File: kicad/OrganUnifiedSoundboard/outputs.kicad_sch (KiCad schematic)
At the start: 9 parts, among them J10 Outputs 53-78, J12 Outputs 79-80, J8 Outputs 1-26, J9 Outputs 27-52

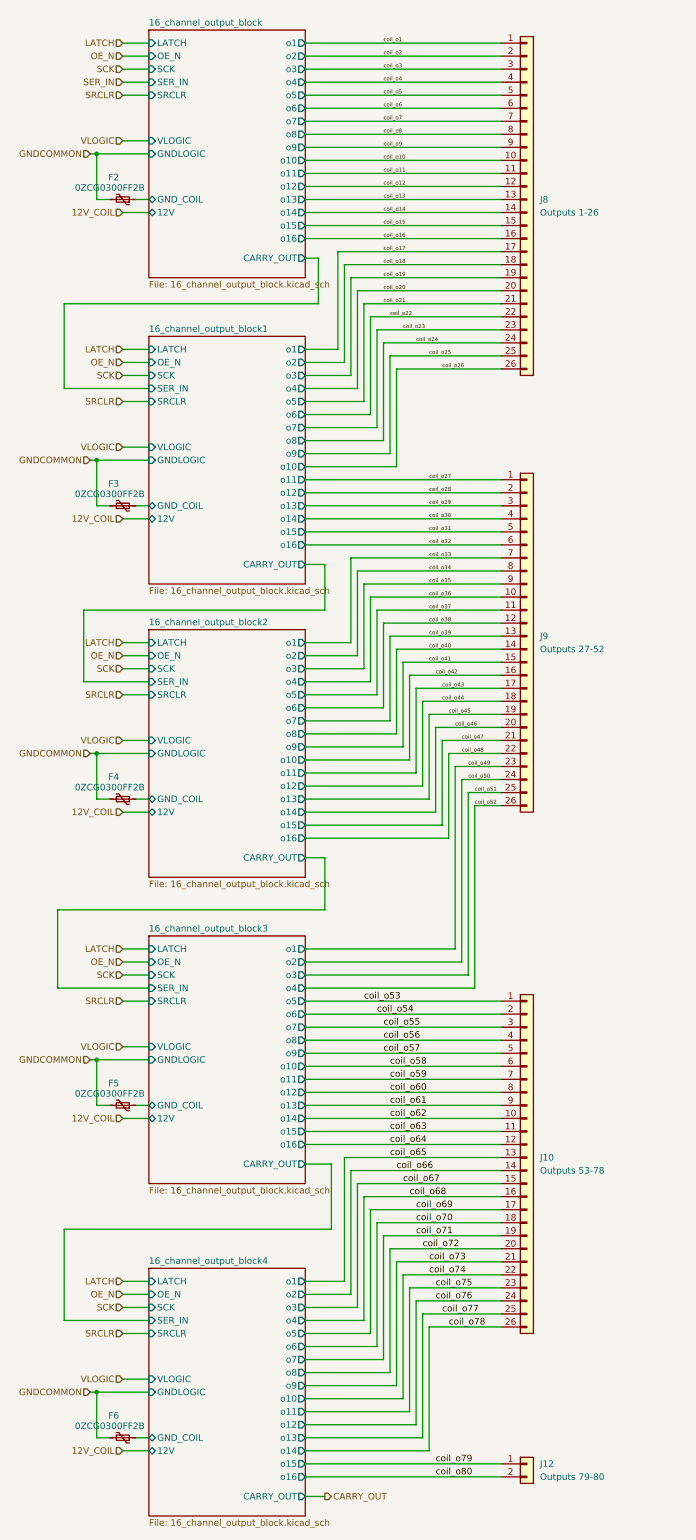
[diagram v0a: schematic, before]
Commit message: Finalized unified soundboard driver for production, adding some models
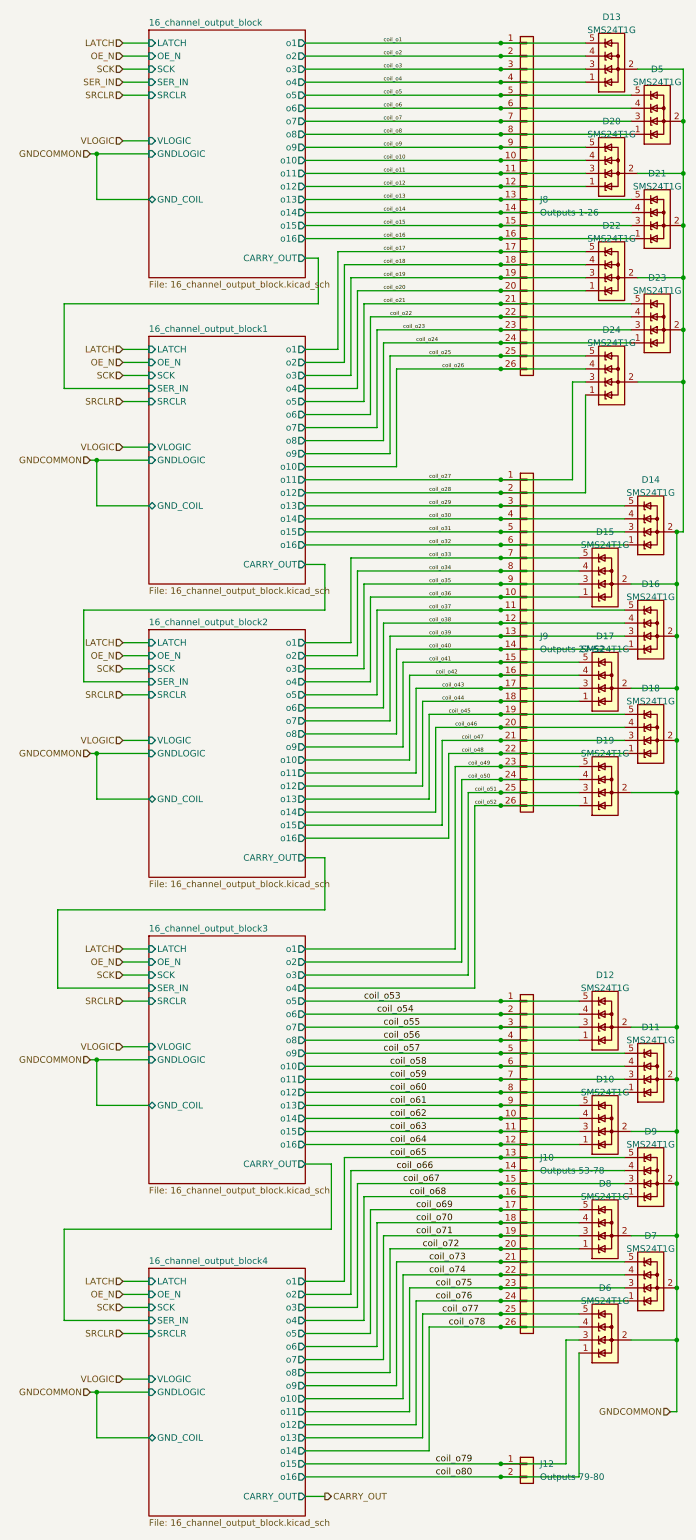
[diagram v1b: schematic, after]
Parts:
- removed F2, F3, F4, F5, F6: 0ZCG0300FF2B, Fuse:Fuse_1812_4532Metric, symbol Device:Polyfuse_Small
- added D10, D11, D12, D13, D14, D15, D16, D17, D18, D19, D20, D21, D22, D23, D24, D5, D6, D7, D8, D9: SMS24T1G, Package_TO_SOT_SMD:SOT-23-5, symbol Power_Protection:SP0504BAHT
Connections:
- net GNDCOMMON: now also D10.2 (A), D11.2 (A), D12.2 (A), D13.2 (A), D14.2 (A), D15.2 (A), D16.2 (A), D17.2 (A), D18.2 (A), D19.2 (A), D20.2 (A), D21.2 (A), D22.2 (A), D23.2 (A), D24.2 (A), D5.2 (A), D6.2 (A), D7.2 (A), D8.2 (A), D9.2 (A)
- net coil_o1: now also D13.5 (K)
- net coil_o10: now also D20.4 (K)
- net coil_o11: now also D20.3 (K)
- net coil_o12: now also D20.1 (K)
- net coil_o13: now also D21.5 (K)
- net coil_o14: now also D21.4 (K)
- net coil_o15: now also D21.3 (K)
- net coil_o16: now also D21.1 (K)
- net coil_o17: now also D22.5 (K)
- net coil_o18: now also D22.4 (K)
- net coil_o19: now also D22.3 (K)
- net coil_o2: now also D13.4 (K)
- net coil_o20: now also D22.1 (K)
- net coil_o21: now also D23.5 (K)
- net coil_o22: now also D23.4 (K)
- net coil_o23: now also D23.3 (K)
- net coil_o24: now also D23.1 (K)
- net coil_o25: now also D24.5 (K)
- net coil_o26: now also D24.4 (K)
- net coil_o27: now also D24.3 (K)
- net coil_o28: now also D24.1 (K)
- net coil_o29: now also D14.5 (K)
- net coil_o3: now also D13.3 (K)
- net coil_o30: now also D14.4 (K)
- net coil_o31: now also D14.3 (K)
- net coil_o32: now also D14.1 (K)
- net coil_o33: now also D15.5 (K)
- net coil_o34: now also D15.4 (K)
- net coil_o35: now also D15.3 (K)
- net coil_o36: now also D15.1 (K)
- net coil_o37: now also D16.5 (K)
- net coil_o38: now also D16.4 (K)
- net coil_o39: now also D16.3 (K)
- net coil_o4: now also D13.1 (K)
- net coil_o40: now also D16.1 (K)
- net coil_o41: now also D17.5 (K)
- net coil_o42: now also D17.4 (K)
- net coil_o43: now also D17.3 (K)
- net coil_o44: now also D17.1 (K)
- net coil_o45: now also D18.5 (K)
- net coil_o46: now also D18.4 (K)
- net coil_o47: now also D18.3 (K)
- net coil_o48: now also D18.1 (K)
- net coil_o49: now also D19.5 (K)
- net coil_o5: now also D5.5 (K)
- net coil_o50: now also D19.4 (K)
- net coil_o51: now also D19.3 (K)
- net coil_o52: now also D19.1 (K)
- net coil_o53: now also D12.5 (K)
- net coil_o54: now also D12.4 (K)
- net coil_o55: now also D12.3 (K)
- net coil_o56: now also D12.1 (K)
- net coil_o57: now also D11.5 (K)
- net coil_o58: now also D11.4 (K)
- net coil_o59: now also D11.3 (K)
- net coil_o6: now also D5.4 (K)
- net coil_o60: now also D11.1 (K)
- net coil_o61: now also D10.5 (K)
- net coil_o62: now also D10.4 (K)
- net coil_o63: now also D10.3 (K)
- net coil_o64: now also D10.1 (K)
- net coil_o65: now also D9.5 (K)
- net coil_o66: now also D9.4 (K)
- net coil_o67: now also D9.3 (K)
- net coil_o68: now also D9.1 (K)
- net coil_o69: now also D8.5 (K)
- net coil_o7: now also D5.3 (K)
- net coil_o70: now also D8.4 (K)
- net coil_o71: now also D8.3 (K)
- net coil_o72: now also D8.1 (K)
- net coil_o73: now also D7.5 (K)
- net coil_o74: now also D7.4 (K)
- net coil_o75: now also D7.3 (K)
- net coil_o76: now also D7.1 (K)
- net coil_o77: now also D6.5 (K)
- net coil_o78: now also D6.4 (K)
- net coil_o79: now also D6.3 (K)
- net coil_o8: now also D5.1 (K)
- net coil_o80: now also D6.1 (K)
- net coil_o9: now also D20.5 (K)
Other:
- sheet 16_channel_output_block ports: added none; removed 12V
- sheet 16_channel_output_block1 ports: added none; removed 12V
- sheet 16_channel_output_block2 ports: added none; removed 12V
- sheet 16_channel_output_block3 ports: added none; removed 12V
- sheet 16_channel_output_block4 ports: added none; removed 12V
